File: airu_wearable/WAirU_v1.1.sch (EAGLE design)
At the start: 49 parts, among them Q2 MMBT3904LT1G, Q3 MMBT3904LT1G, Q6 BSS84, U2 CN3065-DFN8, U3 HDC1080DMBT, U4 PAM2305AABADJ, U6 PAM2401, U7 ESP32_WROOM32_SKINNY

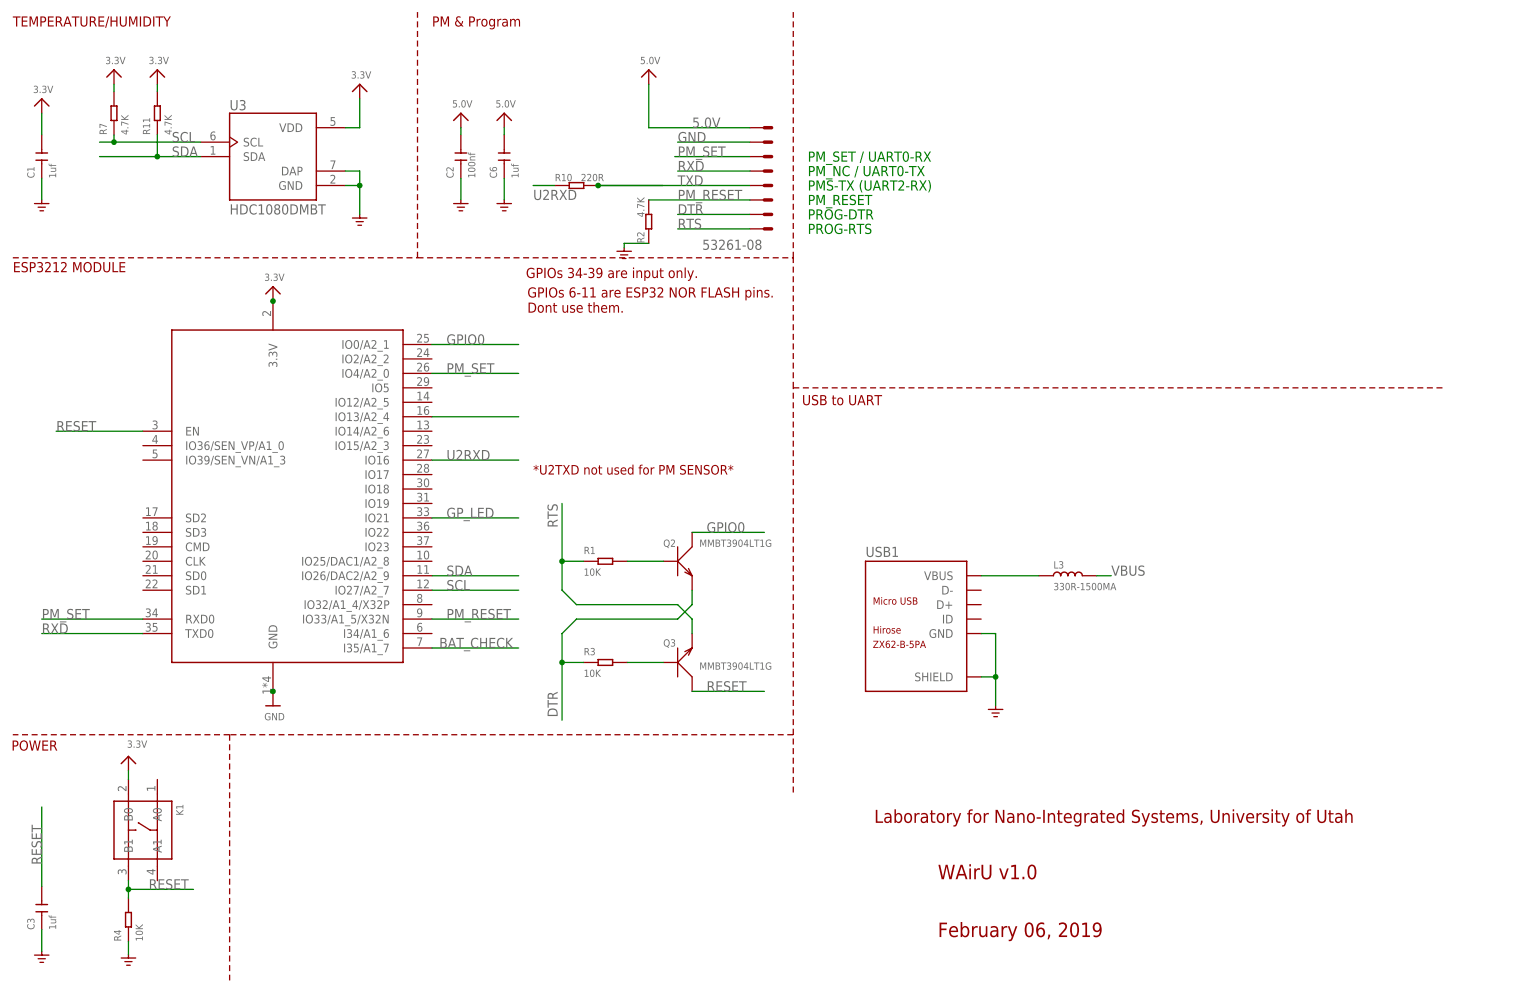
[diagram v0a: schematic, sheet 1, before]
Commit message: Fix Schematic for #9, #10, #11, #12 on github opening issue
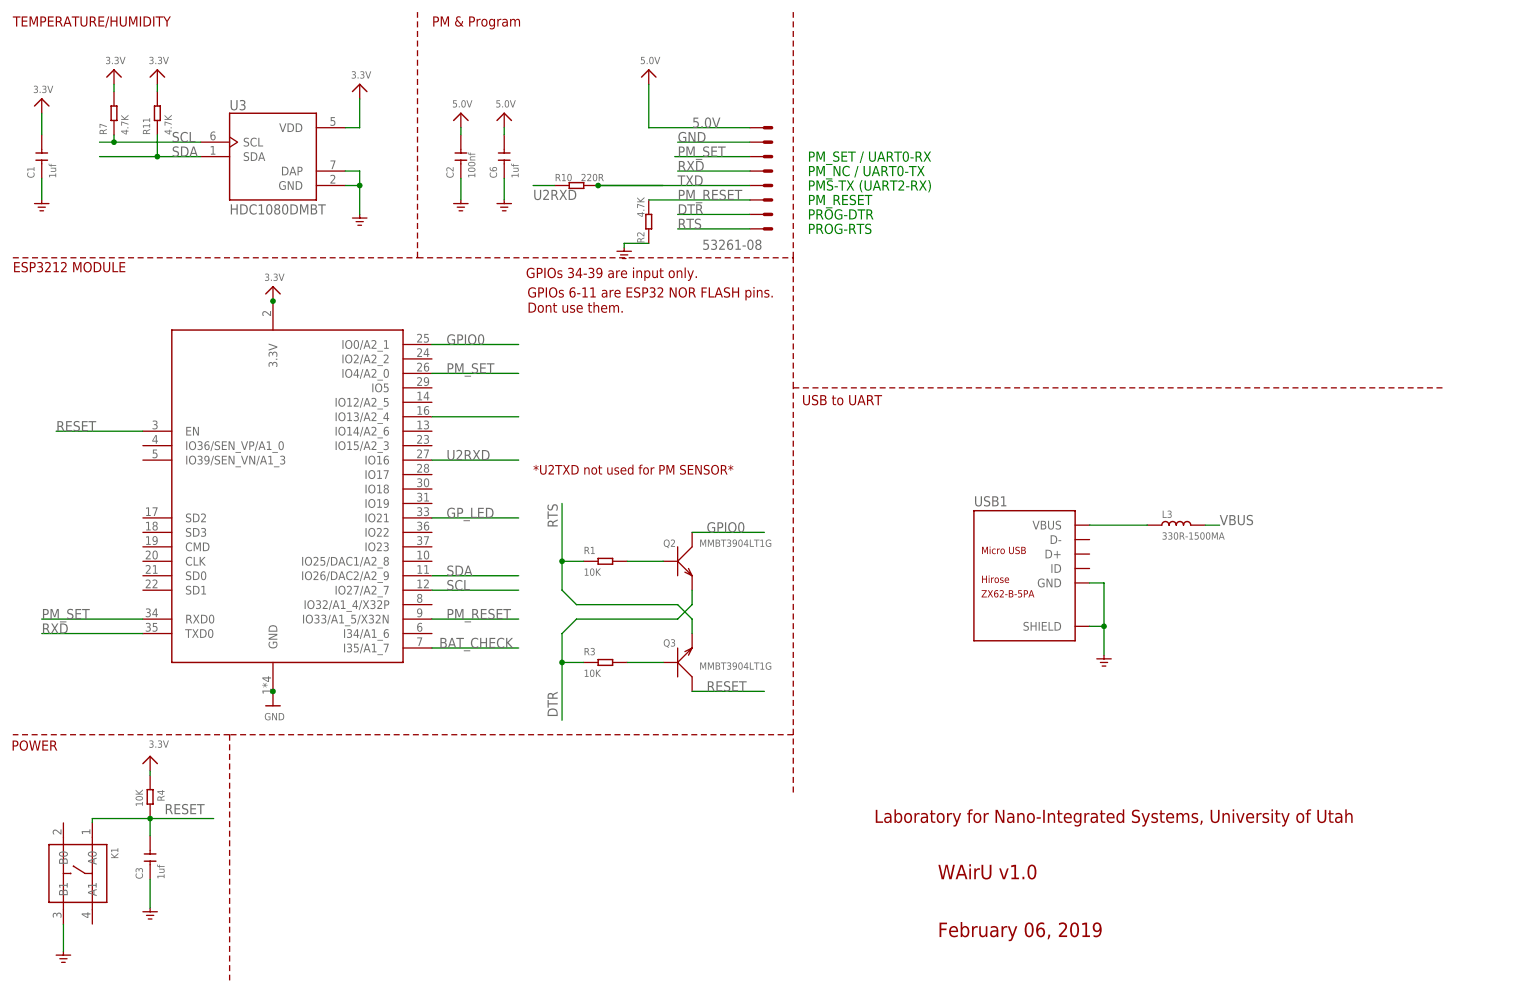
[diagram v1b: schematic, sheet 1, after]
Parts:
- added C5: 100pf, OPL_Capacitor:CERAMIC-100PF-50V-5%-NPO(0603)
- added R8: 2.2K, OPL_Resistor:SMD-RES-2.2K-5%-1/8W(0805)
- added R9: 10K, OPL_Resistor:SMD-RES-10K-1%-1/8W(0805)
- C10, C7, C9: value 22uf -> 10uf
- R12, R13, R22: value 100K -> 100K 1/10W
- R20: value 750K -> 100K 1/10W
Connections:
- new net N$22: C5.1, R8.2, R9.1, U4.BYPASS
- net 3.3V: now also C5.2, R4.1, R9.2; no longer K1.B0, U4.BYPASS
- net GND: now also K1.B1, R8.1; no longer R4.1
- net RESET: now also K1.A0; no longer K1.B1
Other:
- moved on the sheet: C21, C3, K1, L2, L3, R4, TP_3V3, USB1

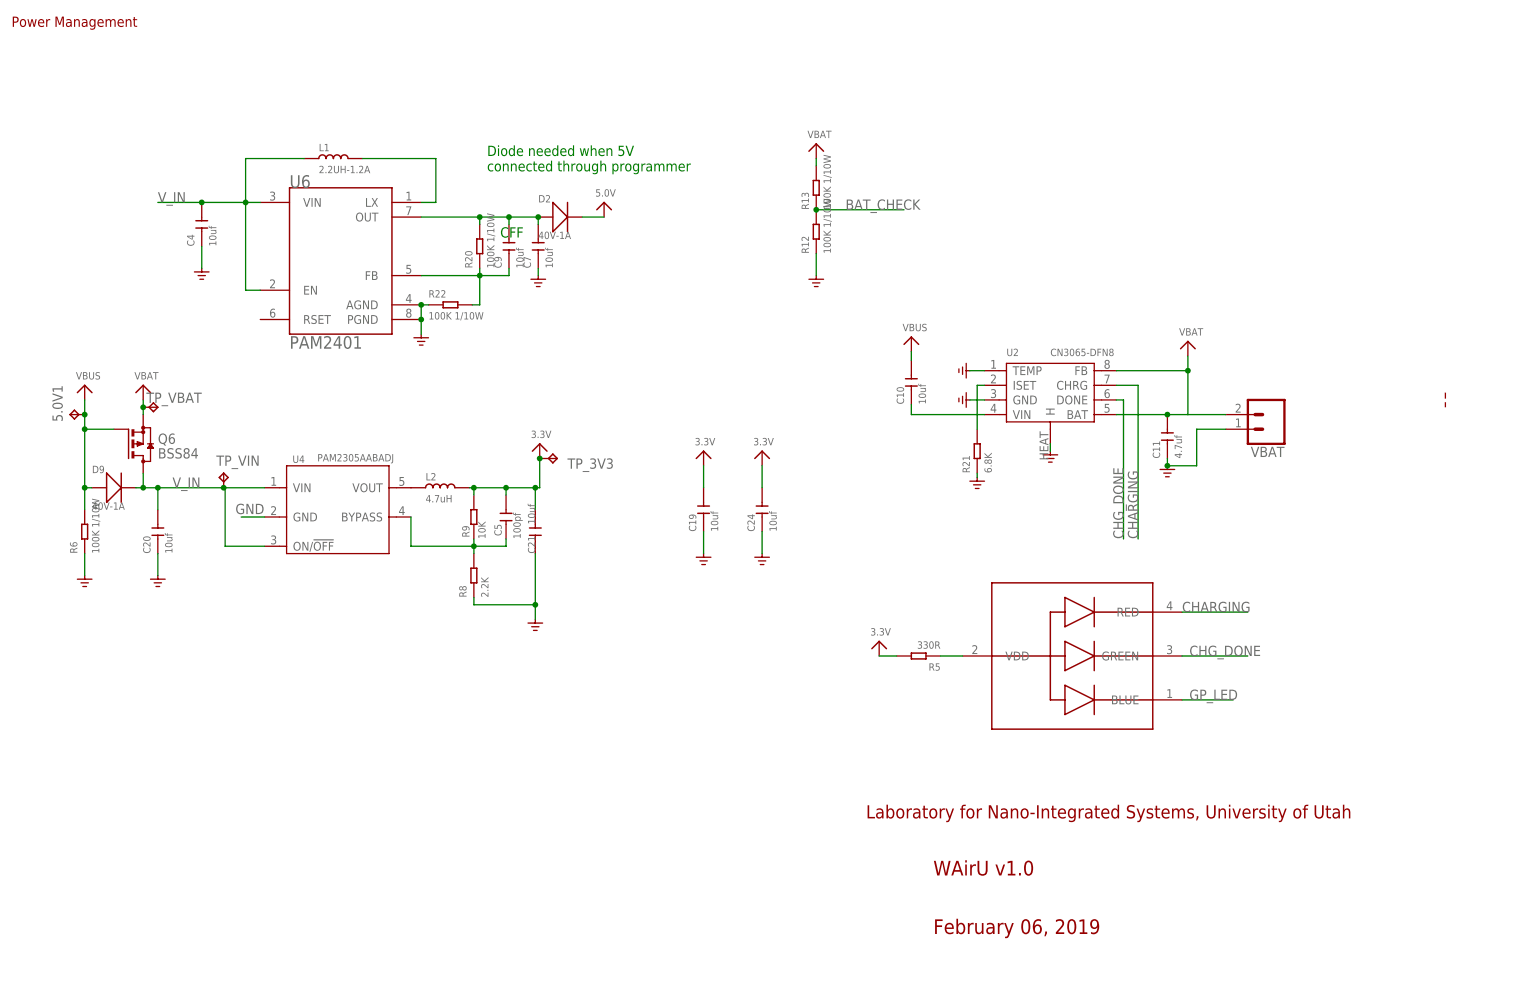
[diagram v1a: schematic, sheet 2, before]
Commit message: Added Switch circuit PAM2401 input for VBUS and VBAT. Added voltage divider for PAM2401 output
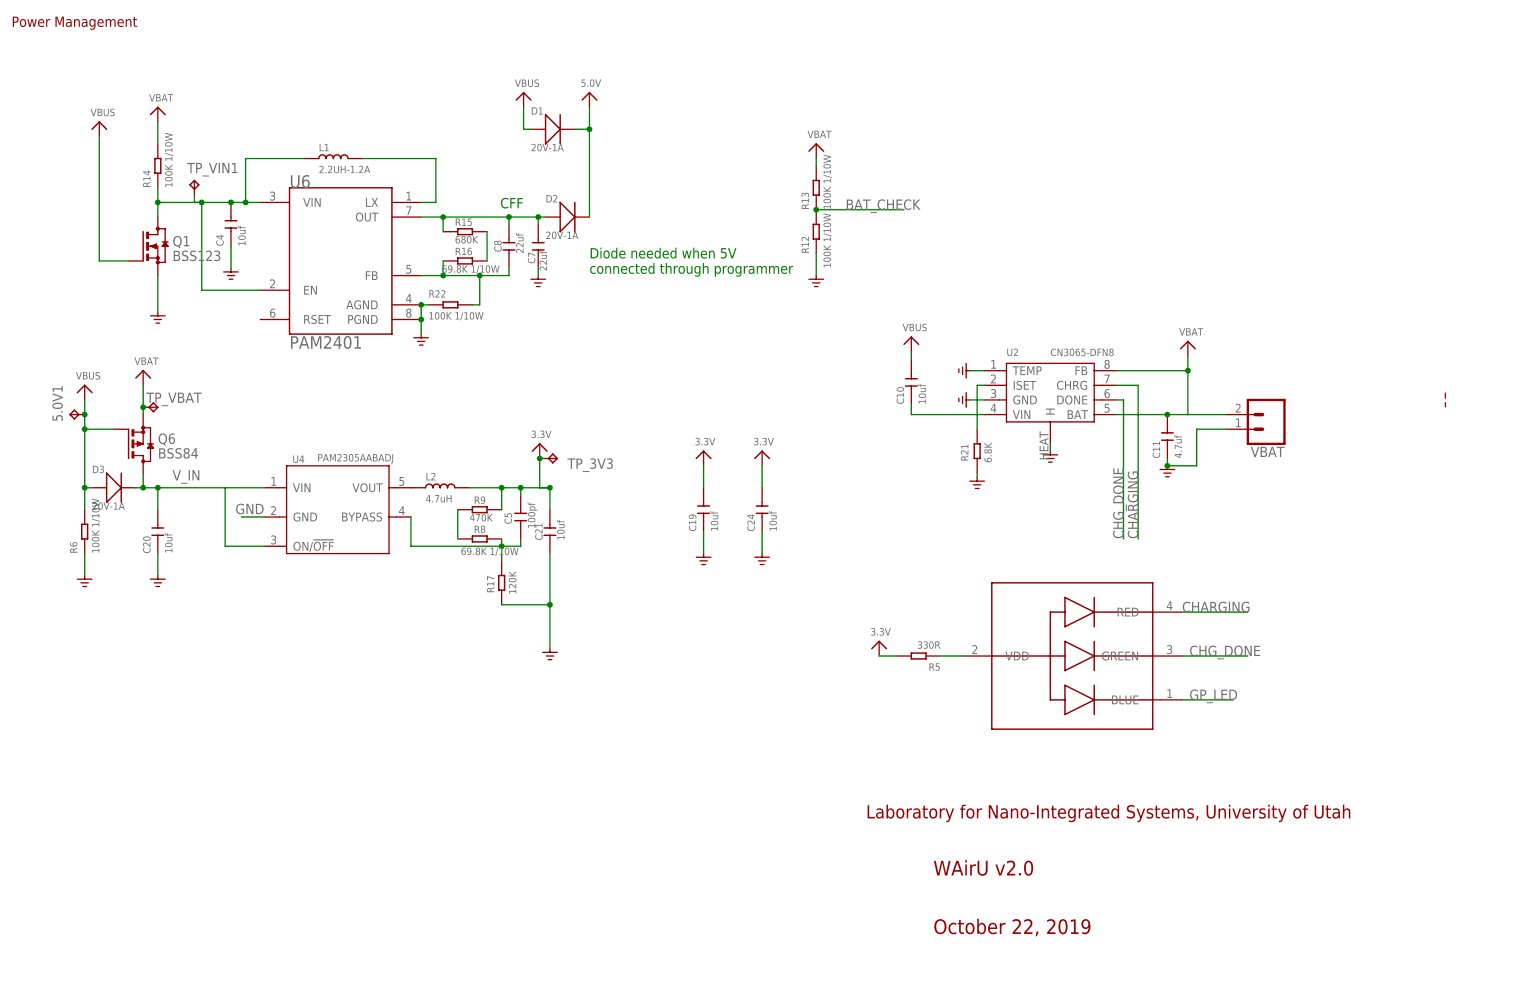
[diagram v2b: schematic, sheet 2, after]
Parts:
- removed D9: 40V-1A, Seeed-Diode:SMD-DIODE-SCHOTTKY-40V-1A(DO-214AC)
- removed R20: 100K 1/10W, OPL_Resistor:SMD-RES-100K-5%-1/10W(0603)
- removed TP_VIN: TPTP20SQ, testpad:TPTP20SQ
- added D1, D3: 20V-1A, Seeed-OPL-Diode:SMD-DIODE-SCHOTTKY-20V-1A(SOD-123)
- added Q1: BSS123, transistor-small-signal:BSS123
- added R14: 100K 1/10W, Seeed-Resistor:SMD-RES-100K-5%-1/10W(0603)
- added R15: 680K, Seeed-OPL-Resistor:SMD-RES-680K-1%-1/16W(0603)
- added R16: 69.8K 1/10W, Seeed-OPL-Resistor:SMD-RES-69.8K-1%-1/10W(0603)
- added R17: 120K, Seeed-OPL-Resistor:SMD-RES-120K-1%-1/10W(0603)
- added TP_VIN1: TPTP20SQ, testpad:TPTP20SQ
- C7, C8: value 10uf -> 22uf
- D2: value 40V-1A -> 20V-1A; device Seeed-Diode:SMD-DIODE-SCHOTTKY-40V-1A(DO-214AC) -> Seeed-OPL-Diode:SMD-DIODE-SCHOTTKY-20V-1A(SOD-123)
- R8: value 2.2K -> 69.8K 1/10W; device OPL_Resistor:SMD-RES-2.2K-5%-1/8W(0805) -> Seeed-OPL-Resistor:SMD-RES-69.8K-1%-1/10W(0603)
- R9: value 10K -> 470K; device OPL_Resistor:SMD-RES-10K-1%-1/8W(0805) -> Seeed-OPL-Resistor:SMD-RES-470K-1%-1/10W(0603)
- renumbered C9 to C8
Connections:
- net PM_SET renamed PM_SET/TXD0
- net RXD renamed RXD0
- net TXD renamed PMS_TX
- new net N$24: R15.2, R16.2
- new net N$67: C4.2, L1.1, Q1.D, R14.1, TP_VIN1.TP, U6.EN, U6.VIN
- new net N$82: R8.1, R9.1
- net 5.0V: now also D1.-
- net GND: now also Q1.S, R17.1; no longer R8.1
- net N$10: now also R16.1; no longer R20.1
- net N$22: now also R17.2; no longer R9.1
- net N$4: now also R15.1; no longer R20.2
- net VBAT: now also R14.2
- net VBUS: now also D1.+, D3.+, Q1.G; no longer D9.+
- net V_IN: now also D3.-; no longer C4.2, D9.-, L1.1, TP_VIN.TP, U6.EN, U6.VIN
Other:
- note added: "October 22, 2019"
- note added: "WAirU v2.0"
- note removed: "February 06, 2019"
- note removed: "WAirU v1.0"
- moved on the sheet: C21, C4, C5, D2, R8, R9

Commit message: 100kOhm PD on Q1 Removed D1 C10 decoupling grounded PMRST to GPIO2 U2RXD to GPIO13
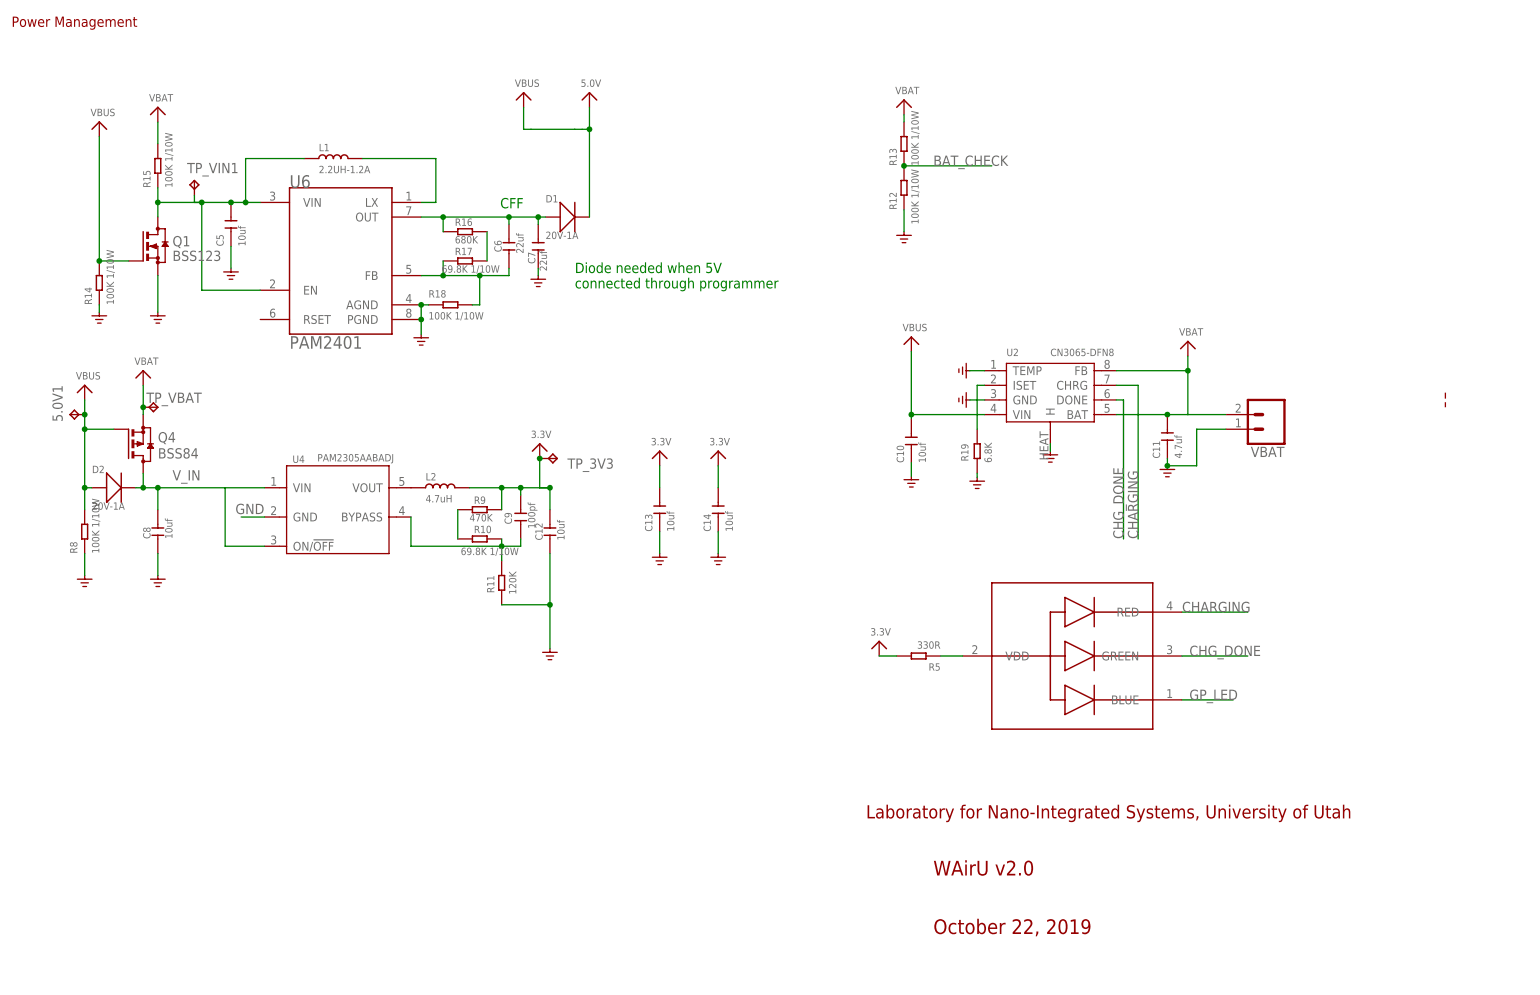
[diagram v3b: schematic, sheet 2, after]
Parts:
- removed C19, C20, C24: 10uf, Seeed-Capacitor:CERAMIC-10UF-10V-10%-X5R(0603)
- removed D3: 20V-1A, Seeed-OPL-Diode:SMD-DIODE-SCHOTTKY-20V-1A(SOD-123)
- added C13, C14: 10uf, Seeed-Capacitor:CERAMIC-10UF-10V-10%-X5R(0603)
- added C9: 100pf, OPL_Capacitor:CERAMIC-100PF-50V-5%-NPO(0603)
- added R20: 10K, Seeed-Resistor:SMD-RES-10K-1%-1/10W(0603)
- C4: value 10uf -> 1uf; device Seeed-Capacitor:CERAMIC-10UF-10V-10%-X5R(0603) -> Seeed-Capacitor:CERAMIC-1UF-25V-10%-X7R(0603)
- C5: value 100pf -> 10uf; device OPL_Capacitor:CERAMIC-100PF-50V-5%-NPO(0603) -> Seeed-Capacitor:CERAMIC-10UF-10V-10%-X5R(0603)
- C6: value 1uf -> 22uf; device Seeed-Capacitor:CERAMIC-1UF-25V-10%-X7R(0603) -> OPL_Capacitor:CERAMIC-10UF-10V-10%-X5R(0603)
- C8: value 22uf -> 10uf; device OPL_Capacitor:CERAMIC-10UF-10V-10%-X5R(0603) -> Seeed-Capacitor:CERAMIC-10UF-10V-10%-X5R(0603)
- R10: value 220R -> 69.8K 1/10W; device Seeed-Resistor:SMD-RES-220R-5%-1/10W(0603) -> Seeed-OPL-Resistor:SMD-RES-69.8K-1%-1/10W(0603)
- R11: value 4.7K -> 120K; device Seeed-Resistor:SMD-RES-4.7K-5%-1/10W(0603) -> Seeed-OPL-Resistor:SMD-RES-120K-1%-1/10W(0603)
- R15: value 680K -> 100K 1/10W; device Seeed-OPL-Resistor:SMD-RES-680K-1%-1/16W(0603) -> Seeed-Resistor:SMD-RES-100K-5%-1/10W(0603)
- R16: value 69.8K 1/10W -> 680K; device Seeed-OPL-Resistor:SMD-RES-69.8K-1%-1/10W(0603) -> Seeed-OPL-Resistor:SMD-RES-680K-1%-1/16W(0603)
- R17: value 120K -> 69.8K 1/10W; device Seeed-OPL-Resistor:SMD-RES-120K-1%-1/10W(0603) -> Seeed-OPL-Resistor:SMD-RES-69.8K-1%-1/10W(0603)
- R2: value 4.7K -> 10K; device Seeed-Resistor:SMD-RES-220R-5%-1/10W(0603) -> Seeed-Resistor:SMD-RES-10K-1%-1/10W(0603)
- R3: value 10K -> 4.7K; device Seeed-Resistor:SMD-RES-10K-1%-1/10W(0603) -> Seeed-Resistor:SMD-RES-220R-5%-1/10W(0603)
- R4: value 10K -> 220R; device Seeed-Resistor:SMD-RES-10K-1%-1/10W(0603) -> Seeed-Resistor:SMD-RES-220R-5%-1/10W(0603)
- R6: value 100K 1/10W -> 4.7K; device Seeed-Resistor:SMD-RES-100K-5%-1/10W(0603) -> Seeed-Resistor:SMD-RES-4.7K-5%-1/10W(0603)
- R8: value 69.8K 1/10W -> 100K 1/10W; device Seeed-OPL-Resistor:SMD-RES-69.8K-1%-1/10W(0603) -> Seeed-Resistor:SMD-RES-100K-5%-1/10W(0603)
- renumbered C21 to C12, Q6 to Q4, R21 to R19, R22 to R18, U$4 to U1
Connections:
- net PM_SET/TXD0 renamed PM_SET/RXD0
- net RXD0 renamed TXD0
- removed net N$5: C10.1, U2.VIN
- removed net N$7: U7.IO13/A2_4
- net 3.3V: now also C13.2, C14.2, C9.2, R20.1, R6.2; no longer C19.2, C24.2, C5.2, R11.2, R4.1
- net 5.0V: now also C3.2; no longer C6.2, D1.-, D2.-
- net DTR: now also R2.1; no longer R3.1
- net GND: now also C10.1, C13.1, C14.1, C5.1, C8.1, R11.1, R14.1, R3.1, R8.1; no longer C19.1, C20.1, C24.1, C6.1, R17.1, R2.1, R6.1
- net N$10: now also C6.1, R17.1; no longer C8.1, R16.1
- net N$12: now also R2.2; no longer R3.2
- net N$22: now also C9.1, R10.2, R11.2; no longer C5.1, R17.2, R8.2
- net N$24: now also R17.2; no longer R15.2
- net N$4: now also C6.2, D1.+, R16.1; no longer C8.2, D2.+, R15.1
- net N$67: now also C5.2, R15.1; no longer C4.2, R14.1
- net N$82: now also R10.1; no longer R8.1
- net PMS_TX: now also R4.2; no longer R10.2
- net PM_RESET: now also R3.2, U7.IO2/A2_2; no longer R2.2, U7.IO33/A1_5/X32N
- net RESET: now also C4.2, R20.2; no longer C3.2, R4.2
- net SCL: now also R6.1; no longer R7.1
- net SDA: now also R7.1; no longer R11.1
- net U2RXD: now also R4.1, U7.IO13/A2_4; no longer R10.1, U7.IO16
- net VBAT: now also R15.2; no longer R14.2
- net VBUS: now also D1.-, D2.+, R14.2, R8.2, U2.VIN; no longer D1.+, D3.+, R6.2
- net V_IN: now also C8.2, D2.-; no longer C20.2, D3.-
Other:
- note added: "Remove RTS line from PMS sensor cable"
- moved on the sheet: C10, C2, C3, C5, C8, D1, D2, R12, R13, R14, R15, R16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
